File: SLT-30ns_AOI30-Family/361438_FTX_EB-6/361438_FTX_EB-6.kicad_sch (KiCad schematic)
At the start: 5 parts, among them T1 IBM_Transistor, T2 IBM_Transistor, T3 IBM_Transistor, T4 IBM_Transistor, U1 12-Pin_SLx_Can

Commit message: Bunch of schematics.
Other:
- note added: "All Transistors ACC"
- note removed: "All Transistors DC"
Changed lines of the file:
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@@
     (stroke (width 0) (type default) (color 0 0 0 0))
   )
-  (text "All Transistors DC" (at 118.11 101.6 0)
+  (text "All Transistors ACC" (at 118.11 101.6 0)
     (effects (font (size 1.27 1.27)) (justify left bottom))
   )
@@
     (pin "3")
   )
+  (symbol (lib_id "IBM_SLT-SLD:IBM_Transistor") (at 165.1 128.27 0) (unit 1)
+    (in_bom yes) (on_board yes) (fields_autoplaced)
+    (property "Reference" "T3" (id 0) (at 168.91 127.6349 0)
+      (effects (font (size 1.27 1.27)) (justify left))
+    )
+    (property "Value" "IBM_Transistor" (id 1) (at 168.91 130.1749 0)
+      (effects (font (size 1.27 1.27)) (justify left))
+    )
+    (property "Footprint" "" (id 2) (at 165.1 128.27 0)
+      (effects (font (size 1.27 1.27)) hide)
+    )
+    (property "Datasheet" "" (id 3) (at 165.1 128.27 0)
+      (effects (font (size 1.27 1.27)) hide)
+    )
+    (pin "1")
+    (pin "2")
+    (pin "3")
+  )
   (symbol (lib_id "IBM_SLT-SLD:12-Pin_SLx_Can") (at 237.49 133.35 0) (unit 1)
     (in_bom yes) (on_board yes) (fields_autoplaced)
@@
     (pin "9")
   )
+  (symbol (lib_id "IBM_SLT-SLD:IBM_Transistor") (at 88.9 73.66 0) (unit 1)
+    (in_bom yes) (on_board yes) (fields_autoplaced)
+    (property "Reference" "T2" (id 0) (at 92.71 73.0249 0)
+      (effects (font (size 1.27 1.27)) (justify left))
+    )
+    (property "Value" "IBM_Transistor" (id 1) (at 92.71 75.5649 0)
+      (effects (font (size 1.27 1.27)) (justify left))
+    )
+    (property "Footprint" "" (id 2) (at 88.9 73.66 0)
+      (effects (font (size 1.27 1.27)) hide)
+    )
+    (property "Datasheet" "" (id 3) (at 88.9 73.66 0)
+      (effects (font (size 1.27 1.27)) hide)
+    )
+    (pin "1")
+    (pin "2")
+    (pin "3")
+  )
   (symbol (lib_id "IBM_SLT-SLD:IBM_Transistor") (at 165.1 73.66 0) (unit 1)
     (in_bom yes) (on_board yes) (fields_autoplaced)
@@
     (pin "3")
   )
-  (symbol (lib_id "IBM_SLT-SLD:IBM_Transistor") (at 88.9 73.66 0) (unit 1)
-    (in_bom yes) (on_board yes) (fields_autoplaced)
-    (property "Reference" "T2" (id 0) (at 92.71 73.0249 0)
-      (effects (font (size 1.27 1.27)) (justify left))
-    )
-    (property "Value" "IBM_Transistor" (id 1) (at 92.71 75.5649 0)
-      (effects (font (size 1.27 1.27)) (justify left))
-    )
-    (property "Footprint" "" (id 2) (at 88.9 73.66 0)
-      (effects (font (size 1.27 1.27)) hide)
-    )
-    (property "Datasheet" "" (id 3) (at 88.9 73.66 0)
-      (effects (font (size 1.27 1.27)) hide)
-    )
-    (pin "1")
-    (pin "2")
-    (pin "3")
-  )
-  (symbol (lib_id "IBM_SLT-SLD:IBM_Transistor") (at 165.1 128.27 0) (unit 1)
-    (in_bom yes) (on_board yes) (fields_autoplaced)
-    (property "Reference" "T3" (id 0) (at 168.91 127.6349 0)
-      (effects (font (size 1.27 1.27)) (justify left))
-    )
-    (property "Value" "IBM_Transistor" (id 1) (at 168.91 130.1749 0)
-      (effects (font (size 1.27 1.27)) (justify left))
-    )
-    (property "Footprint" "" (id 2) (at 165.1 128.27 0)
-      (effects (font (size 1.27 1.27)) hide)
-    )
-    (property "Datasheet" "" (id 3) (at 165.1 128.27 0)
-      (effects (font (size 1.27 1.27)) hide)
-    )
-    (pin "1")
-    (pin "2")
-    (pin "3")
-  )
   (sheet_instances
     (path "/" (page "1"))
   )
   (symbol_instances
-    (path "/1f8e8439-29d6-48dc-85a2-31fc4a1324d9"
+    (path "/2137906f-9d9a-4f2a-b4c3-18311f4a4bdf"
       (reference "T1") (unit 1) (value "IBM_Transistor") (footprint "")
     )
-    (path "/89093827-bb23-4e39-8ebb-d4aae8eed604"
+    (path "/c36f7147-bc6f-4cbe-8b56-617ae1aaead3"
       (reference "T2") (unit 1) (value "IBM_Transistor") (footprint "")
     )
-    (path "/fc223558-0a2b-4b0e-b949-b7fb185c9d35"
+    (path "/313d7939-b1f4-4f95-8fbf-38d2d1bd0a6a"
       (reference "T3") (unit 1) (value "IBM_Transistor") (footprint "")
     )
-    (path "/80f5072b-6b7f-47f8-a9c1-14d05fac811f"
+    (path "/d1e37067-05b9-4eaf-979b-bfe29351874a"
       (reference "T4") (unit 1) (value "IBM_Transistor") (footprint "")
     )

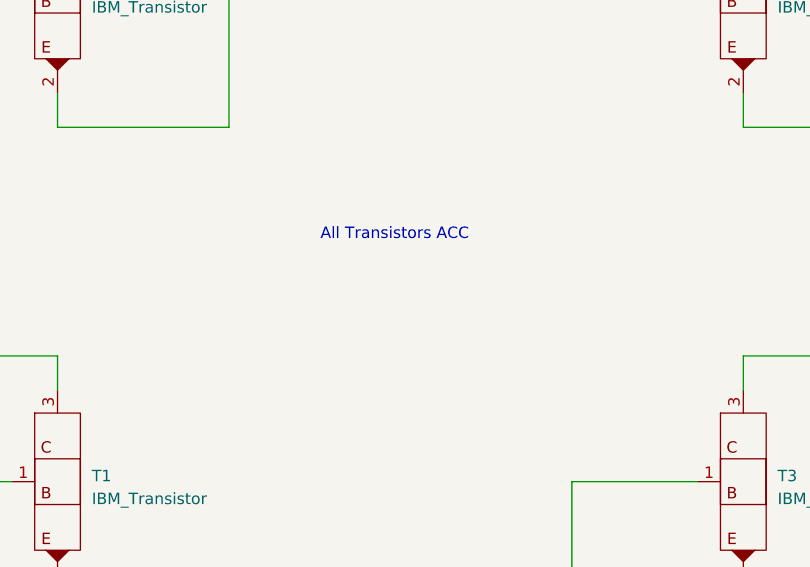
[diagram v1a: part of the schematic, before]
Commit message: Update schematic pdfs
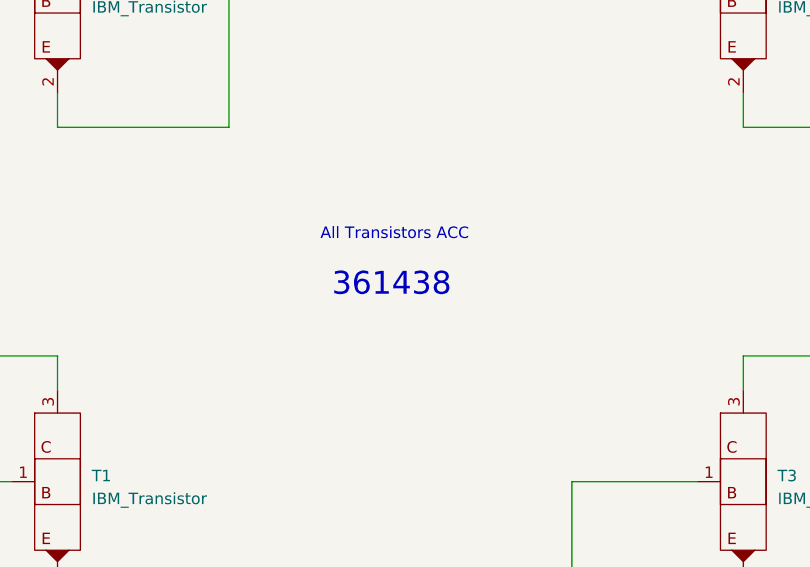
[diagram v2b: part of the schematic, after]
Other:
- note added: "361438"
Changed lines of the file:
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@@
     (stroke (width 0) (type default) (color 0 0 0 0))
+  )
+  (text "361438" (at 119.38 107.95 0)
+    (effects (font (size 2.54 2.54)) (justify left bottom))
   )
   (text "All Transistors ACC" (at 118.11 101.6 0)
